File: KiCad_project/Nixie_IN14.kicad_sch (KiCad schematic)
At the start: 62 parts, among them J1 Conn_01x10_Pin, J2 Conn_01x07_Pin, J3 Conn_01x07_Pin, J4 Conn_01x10_Pin, J5 Conn_01x07_Pin, J6 Conn_01x07_Pin, J7 USB_C_Receptacle_PowerOnly_6P, Q1 IRF540N, Q2 MMBTA42, U1 BME280_module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

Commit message: added missed power capacitors fixed some resistor values continue placing elements on the PCB
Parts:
- added C3, C4: 470uF x 6.3V, Capacitor_THT:CP_Radial_D5.0mm_P2.50mm, symbol Device:C_Polarized
- added C5, C6: 0.1uF, Capacitor_SMD:C_1206_3216Metric, symbol Device:C
- R10: value 100 -> 680k
- R11: value 100 -> 10k
- R8: value 5.1k -> 1k
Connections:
- net +5V: now also C3.1, C4.1, C5.2, C6.2
- net GNDREF: now also C3.2, C4.2, C5.1, C6.1
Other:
- moved on the sheet: U9

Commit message: placing and routing update
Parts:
- removed R1, R2: 330k, Resistor_SMD:R_0805_2012Metric_Pad1.20x1.40mm_HandSolder, symbol Device:R
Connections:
- net LED_R_top: now reaches D1.1 (BA), D2.1 (BA), D3.1 (BA), D4.1 (BA), D5.1 (BA), D6.1 (BA), J3.2 (Pin_2)
- net LED_G_top: now reaches D1.3 (GA), D2.3 (GA), D3.3 (GA), D4.3 (GA), D5.3 (GA), D6.3 (GA), J3.3 (Pin_3)
- net LED_B_top: now reaches D1.4 (RA), D2.4 (RA), D3.4 (RA), D4.4 (RA), D5.4 (RA), D6.4 (RA), J3.4 (Pin_4)
- net LED_B_top: now also J2.7 (Pin_7)
- net A6_top: now reaches J3.7 (Pin_7), N6.A
- net SEC_1_top: now reaches J2.2 (Pin_2)
- net SEC_1_top: now also NE1.2
- net A3_top: now reaches J2.5 (Pin_5), N3.A
- net SEC_2_top: now reaches J3.5 (Pin_5)
- net SEC_2_top: now also NE2.2
- net A5_top: now reaches J3.6 (Pin_6), N5.A
- net A1_top: now reaches J2.3 (Pin_3), N1.A
- net A4_top: now reaches J2.6 (Pin_6), N4.A
- net A2_top: now reaches J2.4 (Pin_4), N2.A
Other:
- moved on the sheet: D1, D2, J2

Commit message: optimized placement for tracing added labels on schematic added capacitor for button
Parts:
- added C7: 0.1uF, Capacitor_SMD:C_1206_3216Metric, symbol Device:C
- D8: footprint Diode_THT:D_DO-41_SOD81_P10.16mm_Horizontal -> Diode_THT:D_DO-41_SOD81_P7.62mm_Horizontal
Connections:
- net BUTTON: now also R4.1, R5.1, U12.1, C7.1
- net GNDREF: now also C7.2
- net A2_DECR: now reaches A1.19 (A0), U10.7 (C)
- net A1_DECR: now reaches A1.20 (A1), U10.6 (B)
- net A3_DECR: now reaches A1.21 (A2), U10.4 (D)
- net A0_DECR: now reaches A1.22 (A3), U10.3 (A)
- net SDA: now reaches A1.23 (A4), U1.4 (SDA), U11.2 (SDA)
- net SCL: now reaches A1.24 (A5), U1.3 (SCL), U11.3 (SCL)
- net 8: now reaches J4.1 (Pin_1), U10.1 (8)
- net 3: now reaches J4.10 (Pin_10), U10.9 (3)
- net 9: now reaches J4.2 (Pin_2), U10.2 (9)
- net 0: now reaches J4.3 (Pin_3), U10.16 (0)
- net 1: now reaches J4.4 (Pin_4), U10.15 (1)
- net 5: now reaches J4.5 (Pin_5), U10.14 (5)
- net 2: now reaches J4.6 (Pin_6), U10.8 (2)
- net 4: now reaches J4.7 (Pin_7), U10.13 (4)
- net 6: now reaches J4.8 (Pin_8), U10.11 (6)
- net 7: now reaches J4.9 (Pin_9), U10.10 (7)
- new net Button: A1.26 (A7)
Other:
- note added: "Mask of board decryptor Set by 'digitMask' variable in the firmware {8, 9, 0, 1, 5, 2, 4, 6, 7, 3}"
- moved on the sheet: A1, BZ1, C1, C2, C3, C4, C5, C6, D7, D8, J4, J5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

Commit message: updated placement started routing
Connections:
- net BUTTON: no longer C7.1, R4.1, R5.1, U12.1
- net GNDREF: no longer D1.2 (K), D2.2 (K), D3.2 (K), D4.2 (K), D5.2 (K), D6.2 (K), J2.1 (Pin_1), J3.1 (Pin_1), NE1.1, NE2.1
- net LED_B: no longer J5.7 (Pin_7)
- net LED_B_top: no longer J2.7 (Pin_7)
- net Button renamed Controls
- net Controls: now also C7.1, R4.1, R5.1, U12.1
- new net GND: D1.2 (K), D2.2 (K), D3.2 (K), D4.2 (K), D5.2 (K), D6.2 (K), J2.1 (Pin_1), J3.1 (Pin_1), NE1.1, NE2.1
- new net LED_B_NCC: J5.7 (Pin_7)
- new net LED_B_top_NC: J2.7 (Pin_7)

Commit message: added 3d models
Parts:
- J1: footprint Connector_PinHeader_2.54mm:PinHeader_1x10_P2.54mm_Vertical -> Connector_PinSocket_2.54mm:PinSocket_1x10_P2.54mm_Vertical
- J2, J3: footprint Connector_PinHeader_2.54mm:PinHeader_1x07_P2.54mm_Vertical -> Connector_PinSocket_2.54mm:PinSocket_1x07_P2.54mm_Vertical
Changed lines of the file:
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@@
 			)
 		)
-		(property "Footprint" "Connector_PinHeader_2.54mm:PinHeader_1x10_P2.54mm_Vertical"
+		(property "Footprint" "Connector_PinSocket_2.54mm:PinSocket_1x10_P2.54mm_Vertical"
 			(at 30.48 87.63 0)
 			(effects
@@
 			)
 		)
-		(property "Footprint" "Connector_PinHeader_2.54mm:PinHeader_1x07_P2.54mm_Vertical"
+		(property "Footprint" "Connector_PinSocket_2.54mm:PinSocket_1x07_P2.54mm_Vertical"
 			(at 450.85 35.56 0)
 			(effects
@@
 			)
 		)
-		(property "Footprint" "Connector_PinHeader_2.54mm:PinHeader_1x07_P2.54mm_Vertical"
+		(property "Footprint" "Connector_PinSocket_2.54mm:PinSocket_1x07_P2.54mm_Vertical"
 			(at 312.42 44.45 0)
 			(effects

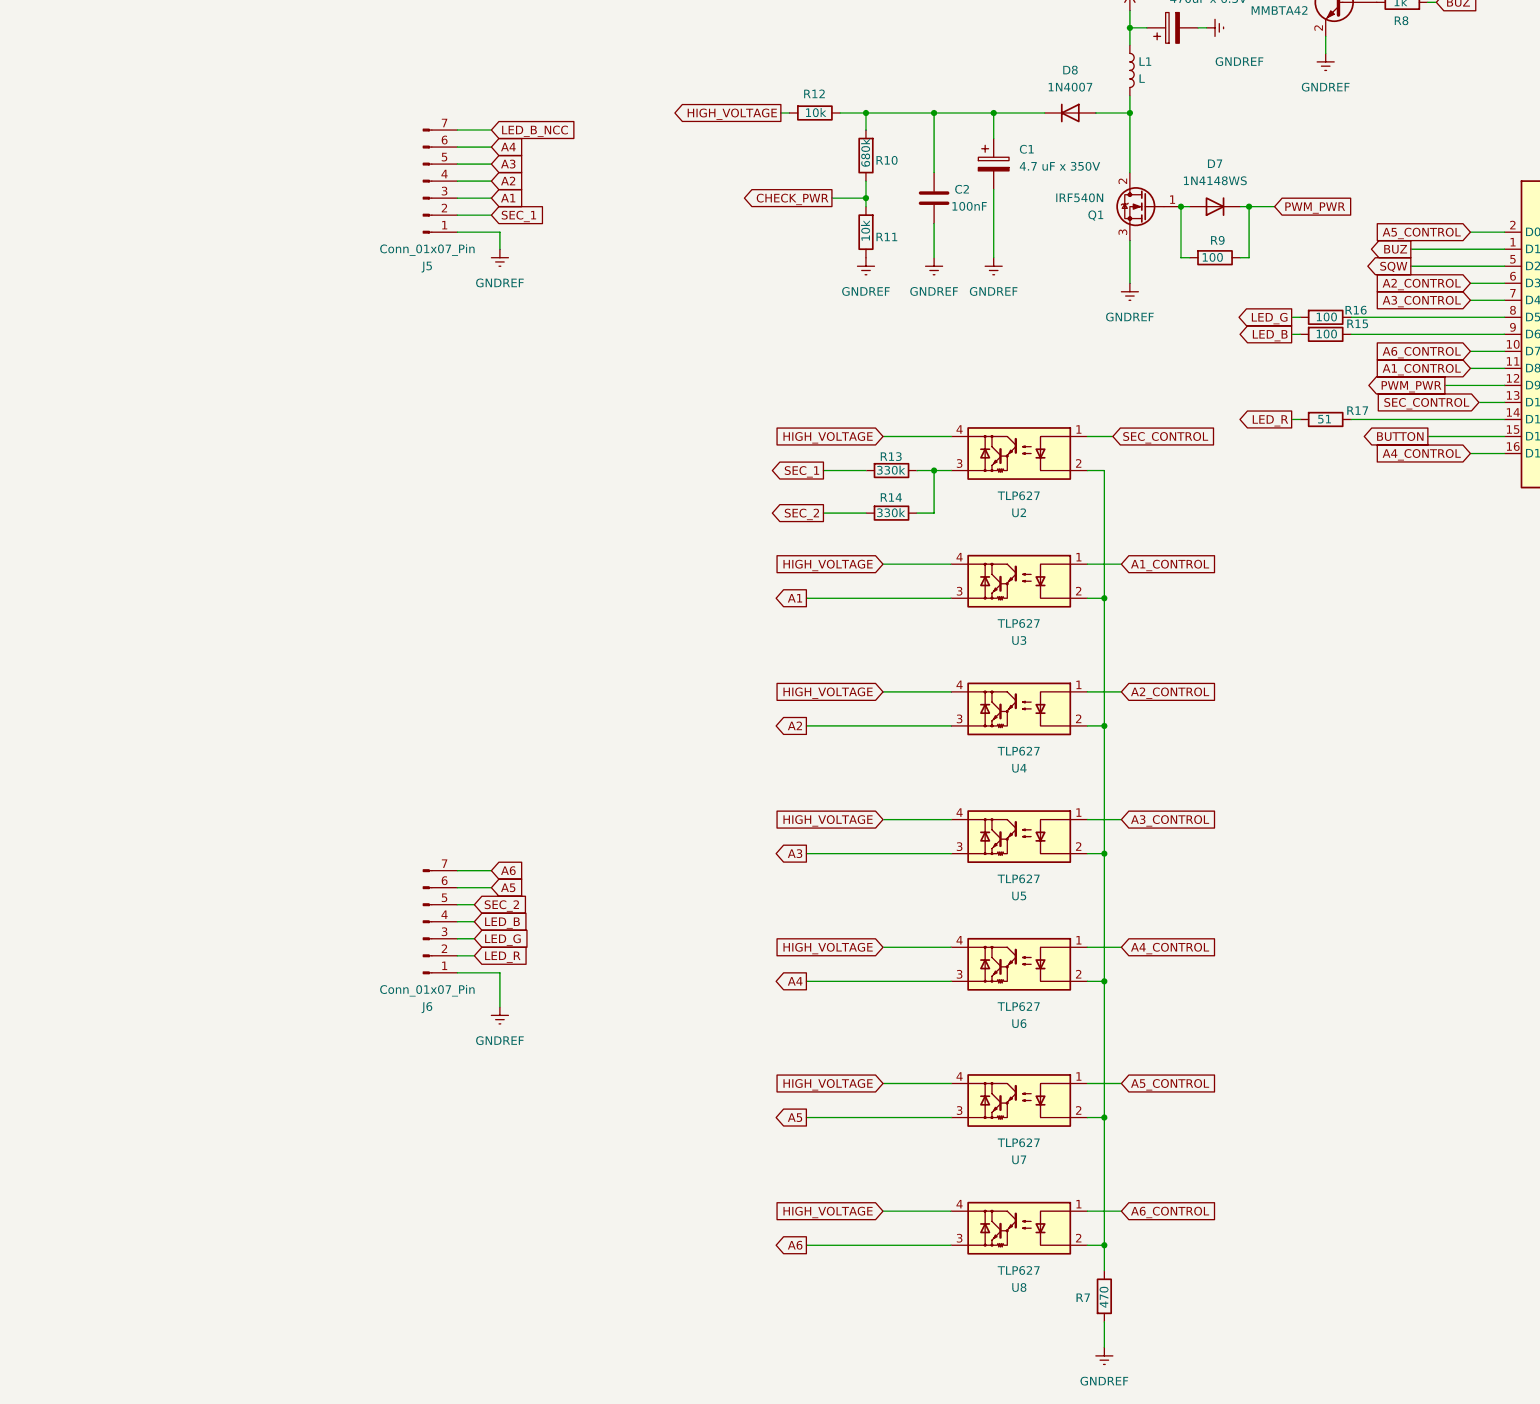
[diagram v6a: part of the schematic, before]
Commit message: placed transistors instead of optic pairs
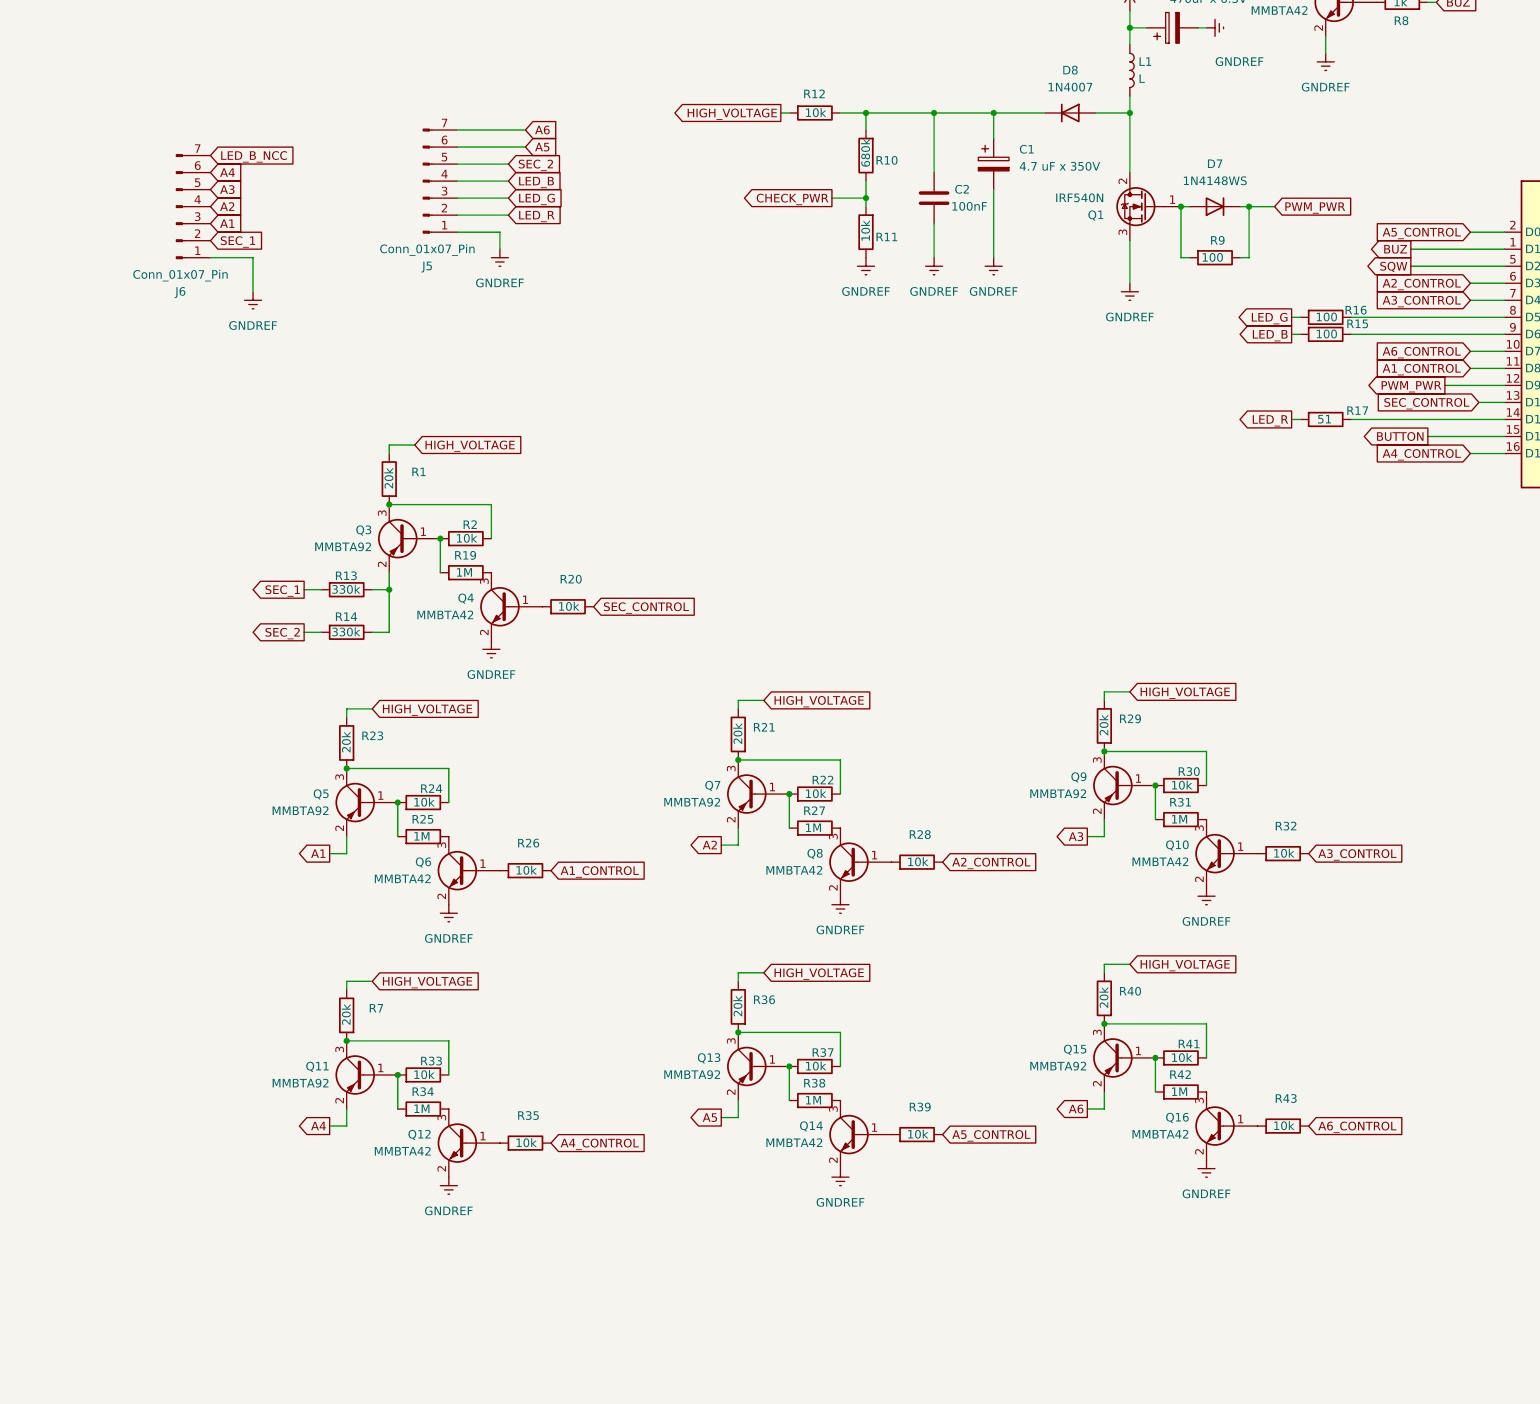
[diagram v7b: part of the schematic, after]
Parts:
- removed U2, U3, U4, U5, U6, U7, U8: TLP627, Package_DIP:DIP-4_W7.62mm, symbol Isolator:TLP627
- added Q10, Q12, Q14, Q16, Q4, Q6, Q8: MMBTA42, Package_TO_SOT_SMD:SOT-23, symbol Transistor_BJT:MMBTA42
- added Q11, Q13, Q15, Q3, Q5, Q7, Q9: MMBTA92, Package_TO_SOT_SMD:SOT-23, symbol Transistor_BJT:MMBTA92
- added R1, R21, R23, R29, R36, R40: 20k, Resistor_SMD:R_0805_2012Metric_Pad1.20x1.40mm_HandSolder, symbol Device:R
- added R19, R25, R27, R31, R34, R38, R42: 1M, Resistor_SMD:R_0805_2012Metric_Pad1.20x1.40mm_HandSolder, symbol Device:R
- added R2, R20, R22, R24, R26, R28, R30, R32, R33, R35, R37, R39, R41, R43: 10k, Resistor_SMD:R_0805_2012Metric_Pad1.20x1.40mm_HandSolder, symbol Device:R
- R7: value 470 -> 20k
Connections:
- net A1: now also J6.3 (Pin_3), Q5.2 (E); no longer J5.3 (Pin_3)
- net A1_CONTROL: now also R26.1
- net A2: now also J6.4 (Pin_4), Q7.2 (E); no longer J5.4 (Pin_4)
- net A2_CONTROL: now also R28.1
- net A3: now also J6.5 (Pin_5), Q9.2 (E); no longer J5.5 (Pin_5)
- net A3_CONTROL: now also R32.1
- net A4: now also J6.6 (Pin_6), Q11.2 (E); no longer J5.6 (Pin_6)
- net A4_CONTROL: now also R35.1
- net A5: now also J5.6 (Pin_6), Q13.2 (E); no longer J6.6 (Pin_6)
- net A5_CONTROL: now also R39.1
- net A6: now also J5.7 (Pin_7), Q15.2 (E); no longer J6.7 (Pin_7)
- net A6_CONTROL: now also R43.1
- net GNDREF: now also Q10.2 (E), Q12.2 (E), Q14.2 (E), Q16.2 (E), Q4.2 (E), Q6.2 (E), Q8.2 (E); no longer R7.2
- net HIGH_VOLTAGE: now also R7.1, R1.1, R21.1, R23.1, R29.1, R36.1, R40.1
- net LED_B: now also J5.4 (Pin_4); no longer J6.4 (Pin_4)
- net LED_B_NCC: now also J6.7 (Pin_7); no longer J5.7 (Pin_7)
- net LED_G: now also J5.3 (Pin_3); no longer J6.3 (Pin_3)
- net LED_R: now also J5.2 (Pin_2); no longer J6.2 (Pin_2)
- net SEC_1: now also J6.2 (Pin_2); no longer J5.2 (Pin_2)
- net SEC_2: now also J5.5 (Pin_5); no longer J6.5 (Pin_5)
- net SEC_CONTROL: now also R20.1
- net at R13.1, R14.1: now also Q3.2 (E)
- new net: Q13.1 (B), R37.2, R38.2
- new net: Q13.3 (C), R36.2, R37.1
- new net: Q8.3 (C), R27.1
- new net: Q7.1 (B), R22.2, R27.2
- new net: Q3.3 (C), R1.2, R2.1
- new net: Q15.1 (B), R41.2, R42.2
- new net: Q15.3 (C), R40.2, R41.1
- new net: Q16.1 (B), R43.2
- new net: Q16.3 (C), R42.1
- new net: Q14.1 (B), R39.2
- new net: Q5.3 (C), R23.2, R24.1
- new net: Q5.1 (B), R24.2, R25.2
- new net: Q12.1 (B), R35.2
- new net: Q12.3 (C), R34.1
- new net: Q6.1 (B), R26.2
- new net: Q6.3 (C), R25.1
- new net: Q11.3 (C), R33.1, R7.2
- new net: Q11.1 (B), R33.2, R34.2
- new net: Q4.3 (C), R19.1
- new net: Q3.1 (B), R19.2, R2.2
- new net: Q8.1 (B), R28.2
- new net: Q4.1 (B), R20.2
- new net: Q10.1 (B), R32.2
- new net: Q7.3 (C), R21.2, R22.1
- new net: Q14.3 (C), R38.1
- new net: Q10.3 (C), R31.1
- new net: Q9.1 (B), R30.2, R31.2
- new net: Q9.3 (C), R29.2, R30.1
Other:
- moved on the sheet: J6, R13, R14
